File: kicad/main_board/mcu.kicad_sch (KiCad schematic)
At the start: 27 parts, among them J2 Conn_01x08, J3 SWD Debug, SW2 RotaryEncoder_Switch, SW3 SW_Push, SW4 SW_Push, SW5 SW_Push, U3 RP2040

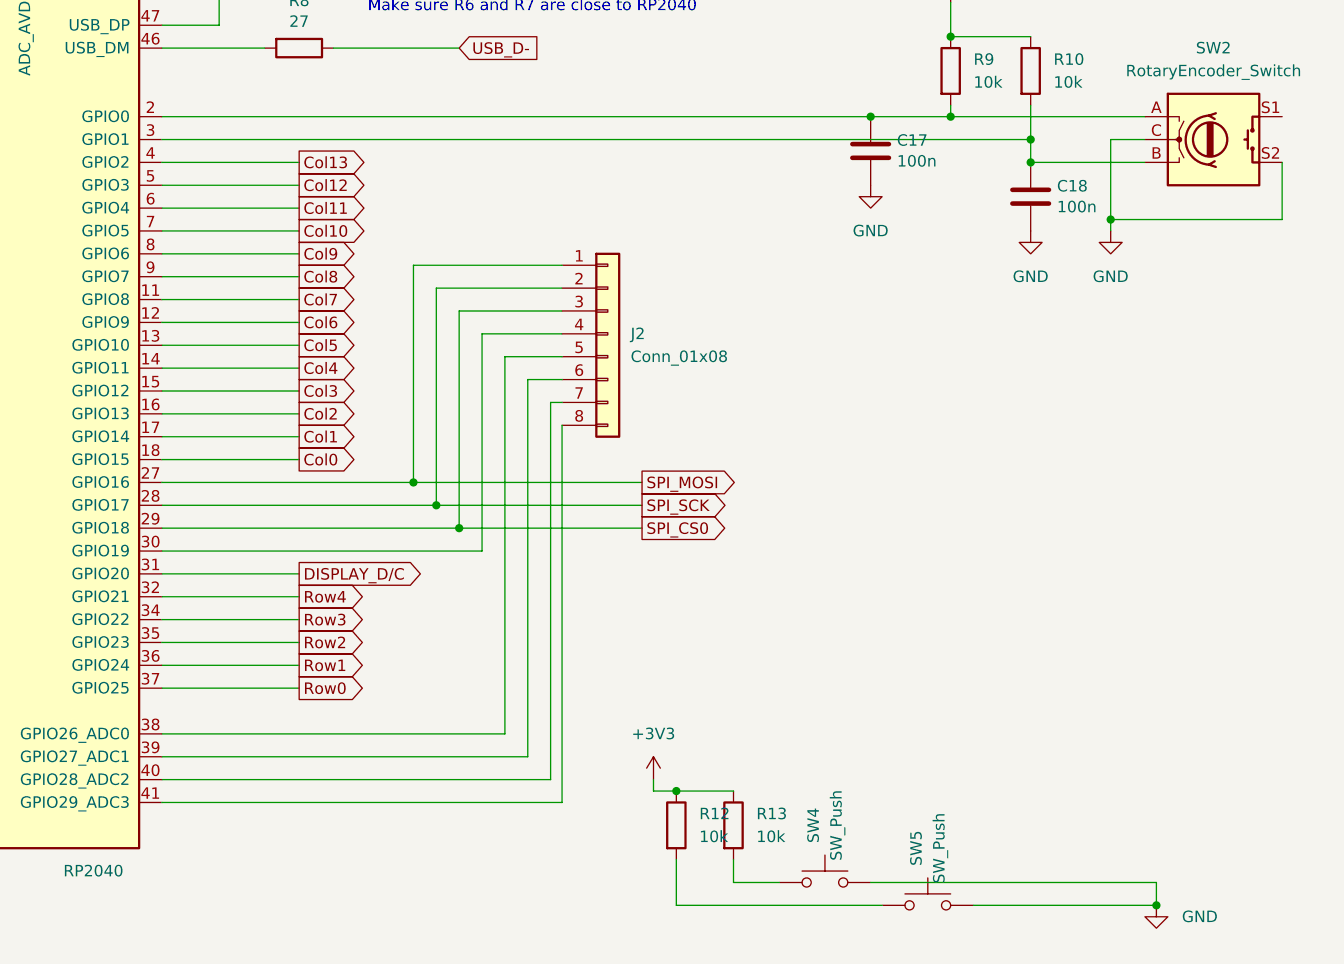
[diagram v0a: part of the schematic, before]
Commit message: separate main board and daughter board
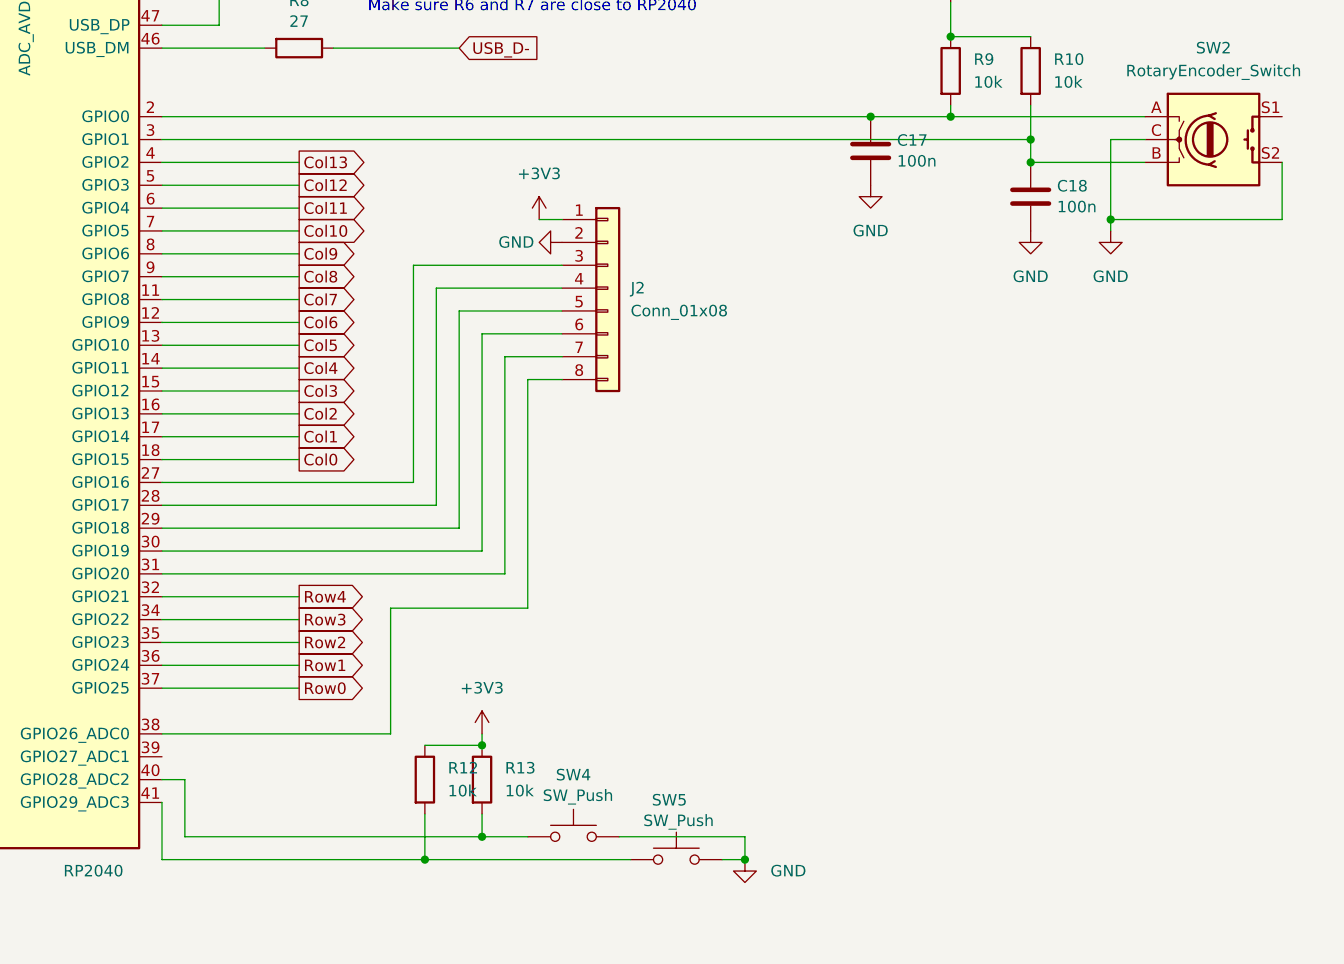
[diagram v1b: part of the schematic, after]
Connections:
- net DISPLAY_D/C is gone; now on an unnamed net: U3.31 (GPIO20)
- net +3V3: now also J2.1 (Pin_1)
- net GND: now also J2.2 (Pin_2)
- net at R12.2, SW5.1: now also U3.41 (GPIO29_ADC3)
- net at J2.4 (Pin_4): now also U3.28 (GPIO17); no longer U3.30 (GPIO19)
- net at J2.5 (Pin_5): now also U3.29 (GPIO18); no longer U3.38 (GPIO26_ADC0)
- net at J2.6 (Pin_6): now also U3.30 (GPIO19); no longer U3.39 (GPIO27_ADC1)
- net at J2.7 (Pin_7): no longer U3.40 (GPIO28_ADC2)
- net at J2.8 (Pin_8): now also U3.38 (GPIO26_ADC0); no longer U3.41 (GPIO29_ADC3)
- net at R13.2, SW4.1: now also U3.40 (GPIO28_ADC2)
- net SPI_CS0: no longer names the net of J2.3 (Pin_3)
- net SPI_CS0: now also U3.27 (GPIO16); no longer U3.29 (GPIO18)
- removed net SPI_MOSI: J2.1 (Pin_1), U3.27 (GPIO16)
- removed net SPI_SCK: J2.2 (Pin_2), U3.28 (GPIO17)
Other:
- moved on the sheet: J2, R12, R13, SW4, SW5
